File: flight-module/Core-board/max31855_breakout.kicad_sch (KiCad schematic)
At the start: 6 parts, among them U2 MAX31855KASA

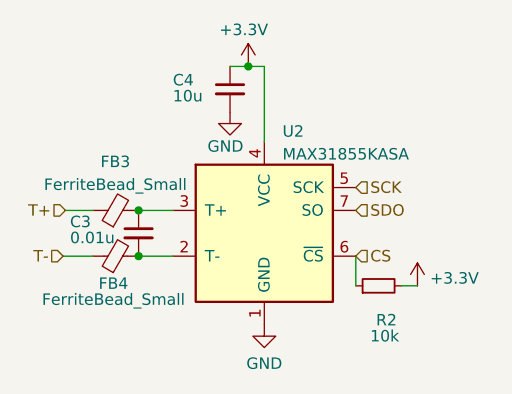
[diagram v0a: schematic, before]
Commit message: worked on core-board schematic. Not done.
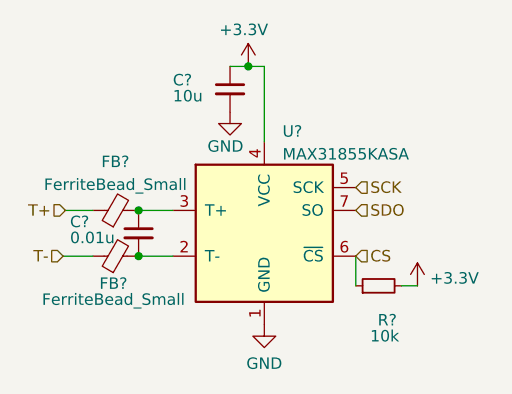
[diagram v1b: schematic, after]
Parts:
- renumbered C3 to C?, C4 to C?, FB4 to FB?, FB3 to FB?, R2 to R?, U2 to U?
